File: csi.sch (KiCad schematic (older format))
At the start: 21 parts, among them J1301 OV5640, SW1301 DPDT, U1301 74LVC1G32, U1302 MIC5504-1.8

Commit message: Add WWAN and WLAN+BT MHF4 coax connectors and antennae symbols to the schematic, remove home and back buttons, reorder sheets so that GNSS is above the haptic motor sheet
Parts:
- C1301: renamed from C1308; value 1uF -> NC
- C1302: renamed from C1310; value 100nF -> NC
- C1303: renamed from C1309; value 1uF -> NC
- R1301: renamed from R1304; value 100k -> NC
- U1301: renamed from U1302; value MIC5504-1.8 -> NC
- renumbered C1301 to C1304, C1302 to C1305, C1303 to C1306, C1304 to C1307, C1305 to C1308, C1307 to C1309, C1306 to C1310, R1301 to R1302, R1302 to R1303, R1303 to R1304, U1301 to U1302
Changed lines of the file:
@@
 DPDT with\nmicrophone
 $Comp
-L R R1301
+L R R1302
 U 1 1 5B1ED51C
 P 7000 2950
-F 0 "R1301" H 7175 3000 50  0000 C CNN
+F 0 "R1302" H 7175 3000 50  0000 C CNN
 F 1 "100k" H 7150 2900 50  0000 C CNN
 F 2 "Resistors_SMD:R_0603" V 6930 2950 50  0001 C CNN
@@
 $EndComp
 $Comp
-L C C1301
+L C C1304
 U 1 1 5B1EAF12
 P 7500 3350
-F 0 "C1301" H 7525 3450 50  0000 L CNN
+F 0 "C1304" H 7525 3450 50  0000 L CNN
 F 1 "10nF" H 7525 3250 50  0000 L CNN
 F 2 "Capacitors_SMD:C_0603" H 7538 3200 50  0001 C CNN
@@
 $EndComp
 $Comp
-L R R1302
+L R R1303
 U 1 1 5B1E9C00
 P 7300 3150
-F 0 "R1302" V 7380 3150 50  0000 C CNN
+F 0 "R1303" V 7380 3150 50  0000 C CNN
 F 1 "100k" V 7200 3150 50  0000 C CNN
 F 2 "Resistors_SMD:R_0603" V 7230 3150 50  0001 C CNN
@@
 $EndComp
 $Comp
-L C C1302
+L C C1305
 U 1 1 5B197A0E
 P 8350 2450
-F 0 "C1302" H 8375 2550 50  0000 L CNN
+F 0 "C1305" H 8375 2550 50  0000 L CNN
 F 1 "100nF" H 8375 2350 50  0000 L CNN
 F 2 "Capacitors_SMD:C_0603" H 8388 2300 50  0001 C CNN
@@
 $EndComp
 $Comp
-L 74LVC1G32 U1301
+L 74LVC1G32 U1302
 U 1 1 5B196213
 P 8700 3050
-F 0 "U1301" H 8700 3100 50  0000 C CNN
+F 0 "U1302" H 8700 3100 50  0000 C CNN
 F 1 "74LVC1G32" H 8700 3000 50  0000 C CNN
 F 2 "" H 8700 3050 50  0001 C CNN
@@
 V_IH(min)=1.26V
 $Comp
-L C C1303
+L C C1306
 U 1 1 5B0F9030
 P 9200 2250
-F 0 "C1303" H 9225 2350 50  0000 L CNN
+F 0 "C1306" H 9225 2350 50  0000 L CNN
 F 1 "100nF" H 9225 2150 50  0000 L CNN
 F 2 "Capacitors_SMD:C_0603" H 9238 2100 50  0001 C CNN
@@
 $EndComp
 $Comp
-L C C1304
+L C C1307
 U 1 1 5B0F8FA9
 P 9450 2250
-F 0 "C1304" H 9450 2350 50  0000 L CNN
+F 0 "C1307" H 9450 2350 50  0000 L CNN
 F 1 "10nF" H 9475 2150 50  0000 L CNN
 F 2 "Capacitors_SMD:C_0603" H 9488 2100 50  0001 C CNN
@@
 $EndComp
 $Comp
-L C C1305
+L C C1308
 U 1 1 5B0F8F0F
 P 9700 2250
-F 0 "C1305" H 9700 2350 50  0000 L CNN
+F 0 "C1308" H 9700 2350 50  0000 L CNN
 F 1 "1nF" H 9725 2150 50  0000 L CNN
 F 2 "Capacitors_SMD:C_0603" H 9738 2100 50  0001 C CNN
@@
 $EndComp
 $Comp
-L C C1306
+L C C1310
 U 1 1 5B0F8E57
 P 9950 2250
-F 0 "C1306" H 9950 2350 50  0000 L CNN
+F 0 "C1310" H 9950 2350 50  0000 L CNN
 F 1 "100pF" H 9950 2150 50  0000 L CNN
 F 2 "Capacitors_SMD:C_0603" H 9988 2100 50  0001 C CNN
@@
 $EndComp
 $Comp
-L C C1307
+L C C1309
 U 1 1 5B2B061C
 P 9750 4450
-F 0 "C1307" H 9775 4550 50  0000 L CNN
+F 0 "C1309" H 9775 4550 50  0000 L CNN
 F 1 "100nF" H 9775 4350 50  0000 L CNN
 F 2 "Capacitors_SMD:C_0603" H 9788 4300 50  0001 C CNN
@@
 OV5640 CMOS Image Sensor Datasheet:\nhttps://cdn.sparkfun.com/datasheets/\nSensors/LightImaging/OV5640_datasheet.pdf
 $Comp
-L MIC5504-1.8YM5 U1302
+L MIC5504-1.8YM5 U1301
 U 1 1 5B313EA0
 P 5300 6400
-F 0 "U1302" H 5125 6725 50  0000 C CNN
-F 1 "MIC5504-1.8" H 5250 6650 50  0000 C CNN
+F 0 "U1301" H 5125 6725 50  0000 C CNN
+F 1 "NC" H 5050 6650 50  0000 C CNN
 F 2 "TO_SOT_Packages_SMD:SOT-23-5" H 5300 6000 50  0001 C CNN
 F 3 "http://ww1.microchip.com/downloads/en/DeviceDoc/MIC550x-300mA-Single-Output-LDO-in-Small-Packages-DS20006006A.pdf" H 5300 6600 50  0001 C CNN
@@
 $EndComp
 $Comp
-L C C1308
+L C C1301
 U 1 1 5B320E3F
 P 4850 6500
-F 0 "C1308" H 4875 6600 50  0000 L CNN
-F 1 "1uF" H 4875 6400 50  0000 L CNN
+F 0 "C1301" H 4875 6600 50  0000 L CNN
+F 1 "NC" H 4875 6400 50  0000 L CNN
 F 2 "Capacitors_SMD:C_0603" H 4888 6350 50  0001 C CNN
 F 3 "" H 4850 6500 50  0001 C CNN
@@
 $EndComp
 $Comp
-L C C1309
+L C C1303
 U 1 1 5B320EA7
 P 5900 6500
-F 0 "C1309" H 5925 6600 50  0000 L CNN
-F 1 "1uF" H 5925 6400 50  0000 L CNN
+F 0 "C1303" H 5925 6600 50  0000 L CNN
+F 1 "NC" H 5925 6400 50  0000 L CNN
 F 2 "Capacitors_SMD:C_0603" H 5938 6350 50  0001 C CNN
 F 3 "" H 5900 6500 50  0001 C CNN
@@
 TODO:\nTest if needed
 $Comp
-L C C1310
+L C C1302
 U 1 1 5B3A47C5
 P 5750 6750
-F 0 "C1310" H 5775 6850 50  0000 L CNN
-F 1 "100nF" H 5775 6650 50  0000 L CNN
+F 0 "C1302" H 5775 6850 50  0000 L CNN
+F 1 "NC" H 5775 6650 50  0000 L CNN
 F 2 "Capacitors_SMD:C_0603" H 5788 6600 50  0001 C CNN
 F 3 "" H 5750 6750 50  0001 C CNN
@@
 $EndComp
 $Comp
-L R R1304
+L R R1301
 U 1 1 5B3A4C79
 P 5750 6100
-F 0 "R1304" H 5925 6150 50  0000 C CNN
-F 1 "100k" H 5900 6050 50  0000 C CNN
+F 0 "R1301" H 5925 6150 50  0000 C CNN
+F 1 "NC" H 5900 6050 50  0000 C CNN
 F 2 "Resistors_SMD:R_0603" V 5680 6100 50  0001 C CNN
 F 3 "" H 5750 6100 50  0001 C CNN
@@
 5ms≤RC≤20ms
 $Comp
-L R R1303
+L R R1304
 U 1 1 5B3A721A
 P 9700 3800
-F 0 "R1303" H 9875 3850 50  0000 C CNN
+F 0 "R1304" H 9875 3850 50  0000 C CNN
 F 1 "10k" H 9825 3750 50  0000 C CNN
 F 2 "Resistors_SMD:R_0603" V 9630 3800 50  0001 C CNN

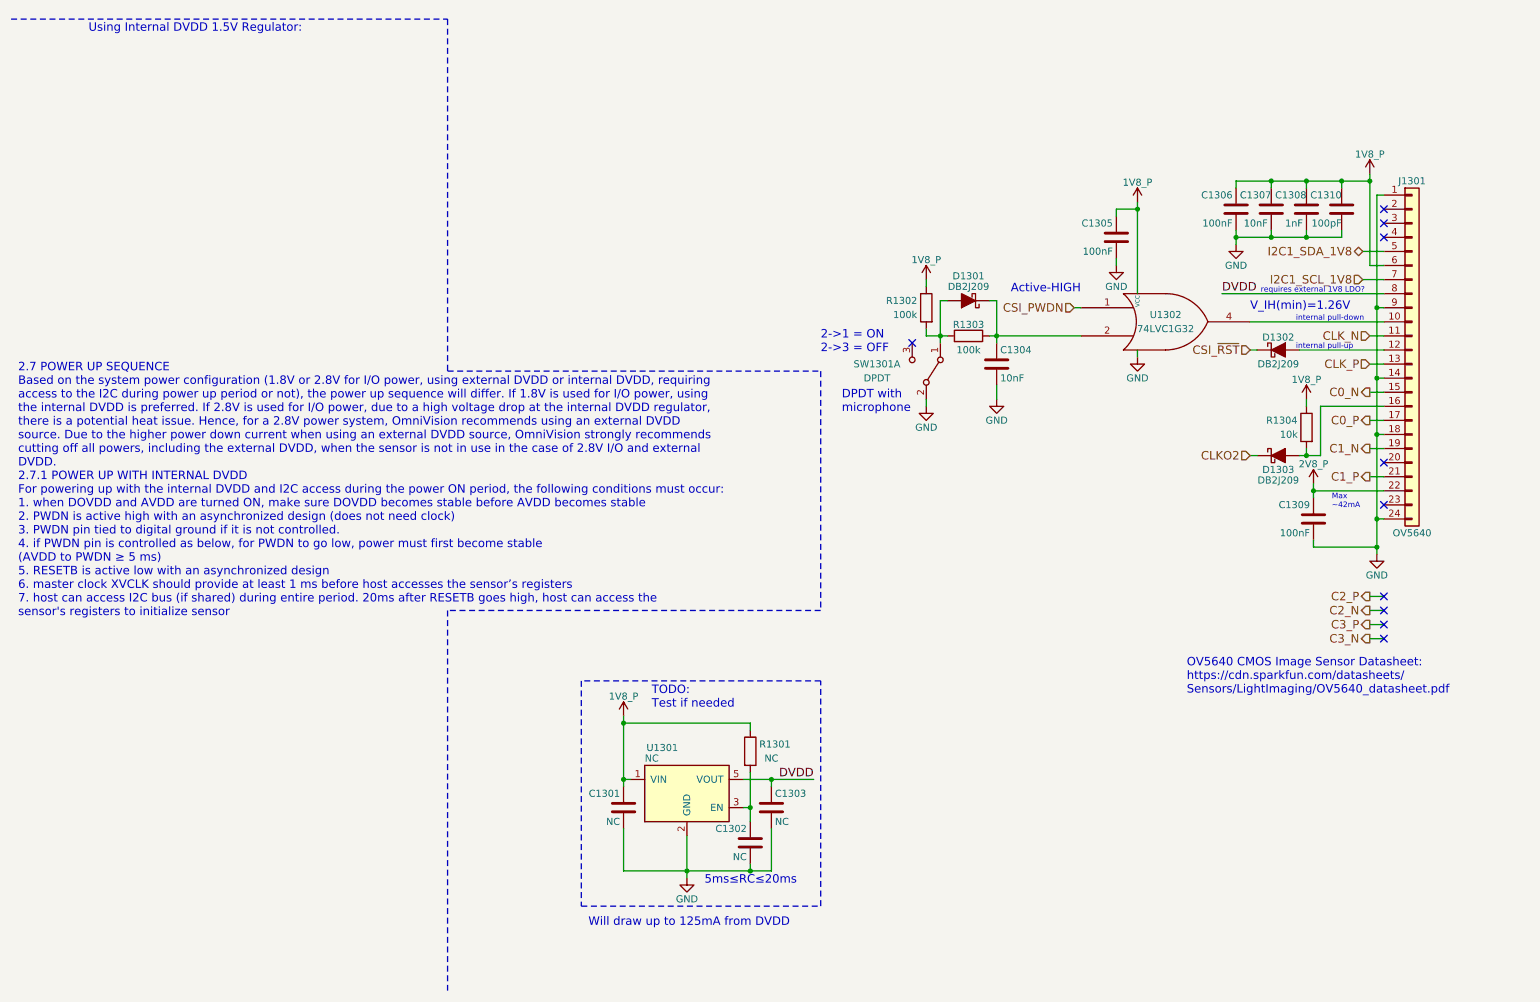
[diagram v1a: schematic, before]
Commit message: Modify the CSI circuit to use a 02x15 connector for potential use with the CO8725-B5SA-E camera, include cap touch FPC connector details, make minor adjustments to GNSS antenna circuit
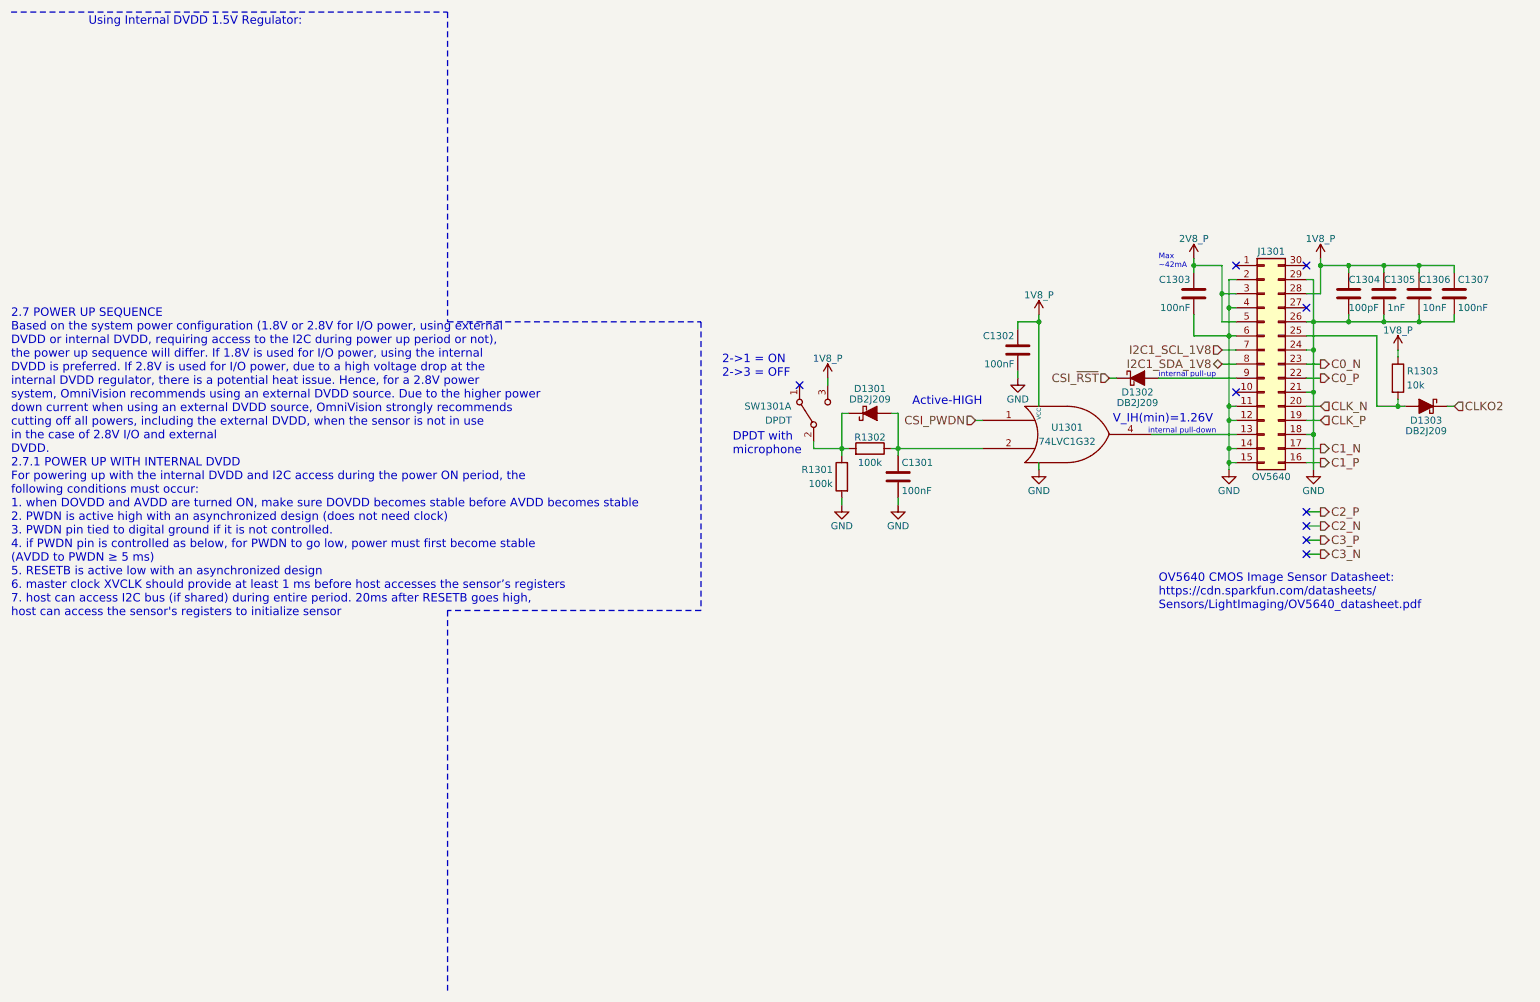
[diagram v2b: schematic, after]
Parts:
- removed C1301, C1302, C1303: NC, Capacitors_SMD:C_0603, symbol C
- removed J1301: OV5640, symbol Conn_01x24
- removed R1301: NC, Resistors_SMD:R_0603, symbol R
- removed U1301: NC, TO_SOT_Packages_SMD:SOT-23-5, symbol MIC5504-1.8YM5
- added J1301: OV5640, symbol Conn_02x15_Counter_Clockwise
- C1301: renamed from C1304; value 10nF -> 100nF
- renumbered C1305 to C1302, C1309 to C1303, C1310 to C1304, C1308 to C1305, C1307 to C1306, C1306 to C1307, R1302 to R1301, R1303 to R1302, R1304 to R1303, U1302 to U1301
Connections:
- net 1V8_P: now also SW1301.3 (C), J1301.28 (Pin_28); no longer R1301.1
- net 2V8_P: now also J1301.3 (Pin_3), J1301.5 (Pin_5)
- net C0_N: now also J1301.23 (Pin_23)
- net C0_P: now also J1301.22 (Pin_22)
- net C1_N: now also J1301.17 (Pin_17)
- net C1_P: now also J1301.16 (Pin_16)
- net CLK_N: now also J1301.20 (Pin_20)
- net CLK_P: now also J1301.19 (Pin_19)
- net GND: now also R1301.2, J1301.11 (Pin_11), J1301.12 (Pin_12), J1301.14 (Pin_14), J1301.15 (Pin_15), J1301.18 (Pin_18), J1301.2 (Pin_2), J1301.21 (Pin_21), J1301.24 (Pin_24), J1301.26 (Pin_26), J1301.29 (Pin_29), J1301.4 (Pin_4), J1301.6 (Pin_6); no longer SW1301.2 (B)
- net I2C1_SCL_1V8: now also J1301.7 (Pin_7)
- net I2C1_SDA_1V8: now also J1301.8 (Pin_8)
- net at U1301.4: now also J1301.13 (Pin_13)
- net at D1302.2 (A): now also J1301.9 (Pin_9)
- net at D1303.2 (A), R1303.2: now also J1301.25 (Pin_25)
- net at C1301.1, R1302.1, U1301.2: now also D1301.2 (A); no longer D1301.1 (K)
- new net: D1301.1 (K), R1301.1, R1302.2, SW1301.2 (B)
- now unconnected: SW1301.1 (A)
- no-connect marks 10 -> 9
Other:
- note added: "2.7 POWER UP SEQUENCE\nBased on the system power configuration (1.8V or 2.8V for I/O power, using external\nDVDD or internal DVDD, requiring access to the I2C during power up period or not),\nthe power up sequence will differ. If 1.8V is used for I/O power, using the internal\nDVDD is preferred. If 2.8V is used for I/O power, due to a high voltage drop at the\ninternal DVDD regulator, there is a 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"
- note removed: "2.7 POWER UP SEQUENCE\nBased on the system power configuration (1.8V or 2.8V for I/O power, using external DVDD or internal DVDD, requiring\naccess to the I2C during power up period or not), the power up sequence will differ. If 1.8V is used for I/O power, using\nthe internal DVDD is preferred. If 2.8V is used for I/O power, due to a high voltage drop at the internal DVDD regulator,\nthere is a p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"
- note removed: "5ms≤RC≤20ms"
- note removed: "TODO:\nTest if needed"
- note removed: "Will draw up to 125mA from DVDD"
- note removed: "requires external 1V8 LDO?"
- moved on the sheet: C1301, C1302, C1303, C1304, C1305, C1306, C1307, D1301, D1302, D1303, R1301, R1302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

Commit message: Include address in schematic notes for all I2C1 slaves, make HDMI connector shielding resistor to GND 0Ohms
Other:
- note added: "Slave Address: 0x78"
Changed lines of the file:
@@
 	10750 3050 10750 3000
 Connection ~ 10000 3050
+Text Notes 9000 2300 0    60   ~ 0
+Slave Address: 0x78
 $EndSCHEMATC

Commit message: Add notes regarding I2C's 3V3_OUT supply and the fact that it is sourced from NVCC_3P3 (3A BUCK6), add additional notes regarding the RTC and Camera's I2C slave address, reannotate the whole schematic (nearly the last time)
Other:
- note added: "7-bit Slave Address: 0x78\n (1111 000x)"
- note added: "Read: 0xF1\nWrite 0xF0"
- note removed: "Slave Address: 0x78"
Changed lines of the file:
@@
 Sheet 13 24
 Title ""
-Date "2018-05-23"
+Date "2018-05-31"
 Rev "v0.1.0"
 Comp "Purism SPC"
@@
 $EndComp
 $Comp
-L GND #PWR0194
+L GND #PWR1303
 U 1 1 5B1EAF19
 P 6800 4350
-F 0 "#PWR0194" H 6800 4100 50  0001 C CNN
+F 0 "#PWR1303" H 6800 4100 50  0001 C CNN
 F 1 "GND" H 6800 4200 50  0000 C CNN
 F 2 "" H 6800 4350 50  0001 C CNN
@@
 $EndComp
 $Comp
-L 1V8_P #PWR0195
+L 1V8_P #PWR1301
 U 1 1 5B1DBE6F
 P 6300 3450
-F 0 "#PWR0195" H 6300 3300 50  0001 C CNN
+F 0 "#PWR1301" H 6300 3300 50  0001 C CNN
 F 1 "1V8_P" H 6300 3590 50  0000 C CNN
 F 2 "" H 6300 3450 50  0001 C CNN
@@
 $EndComp
 $Comp
-L GND #PWR0196
+L GND #PWR1304
 U 1 1 5B1A278C
 P 7650 3450
-F 0 "#PWR0196" H 7650 3200 50  0001 C CNN
+F 0 "#PWR1304" H 7650 3200 50  0001 C CNN
 F 1 "GND" H 7650 3300 50  0000 C CNN
 F 2 "" H 7650 3450 50  0001 C CNN
@@
 $EndComp
 $Comp
-L GND #PWR0197
+L GND #PWR1306
 U 1 1 5B1964B5
 P 7800 4100
-F 0 "#PWR0197" H 7800 3850 50  0001 C CNN
+F 0 "#PWR1306" H 7800 3850 50  0001 C CNN
 F 1 "GND" H 7800 3950 50  0000 C CNN
 F 2 "" H 7800 4100 50  0001 C CNN
@@
 CLKO2
 $Comp
-L 1V8_P #PWR0198
+L 1V8_P #PWR1311
 U 1 1 5B105CDE
 P 10350 3250
-F 0 "#PWR0198" H 10350 3100 50  0001 C CNN
+F 0 "#PWR1311" H 10350 3100 50  0001 C CNN
 F 1 "1V8_P" H 10350 3390 50  0000 C CNN
 F 2 "" H 10350 3250 50  0001 C CNN
@@
 $EndComp
 $Comp
-L 1V8_P #PWR0199
+L 1V8_P #PWR1310
 U 1 1 5B0F8E1D
 P 9800 2600
-F 0 "#PWR0199" H 9800 2450 50  0001 C CNN
+F 0 "#PWR1310" H 9800 2450 50  0001 C CNN
 F 1 "1V8_P" H 9800 2740 50  0000 C CNN
 F 2 "" H 9800 2600 50  0001 C CNN
@@
 C0_P
 $Comp
-L 1V8_P #PWR0200
+L 1V8_P #PWR1305
 U 1 1 5B19049B
 P 7800 3000
-F 0 "#PWR0200" H 7800 2850 50  0001 C CNN
+F 0 "#PWR1305" H 7800 2850 50  0001 C CNN
 F 1 "1V8_P" H 7800 3140 50  0000 C CNN
 F 2 "" H 7800 3000 50  0001 C CNN
@@
 $EndComp
 $Comp
-L 2V8_P #PWR0201
+L 2V8_P #PWR1307
 U 1 1 5B2B0429
 P 8900 2600
-F 0 "#PWR0201" H 8900 2450 50  0001 C CNN
+F 0 "#PWR1307" H 8900 2450 50  0001 C CNN
 F 1 "2V8_P" H 8900 2740 50  0000 C CNN
 F 2 "" H 8900 2600 50  0001 C CNN
@@
 NoConn ~ 9200 2650
 $Comp
-L GND #PWR0202
+L GND #PWR1308
 U 1 1 5B11F1A4
 P 9150 4100
-F 0 "#PWR0202" H 9150 3850 50  0001 C CNN
+F 0 "#PWR1308" H 9150 3850 50  0001 C CNN
 F 1 "GND" H 9150 3950 50  0000 C CNN
 F 2 "" H 9150 4100 50  0001 C CNN
@@
 NoConn ~ 9200 3550
 $Comp
-L GND #PWR0203
+L GND #PWR1309
 U 1 1 5B11FD52
 P 9750 4100
-F 0 "#PWR0203" H 9750 3850 50  0001 C CNN
+F 0 "#PWR1309" H 9750 3850 50  0001 C CNN
 F 1 "GND" H 9750 3950 50  0000 C CNN
 F 2 "" H 9750 4100 50  0001 C CNN
@@
 	9800 2600 9800 2850
 $Comp
-L GND #PWR0204
+L GND #PWR1302
 U 1 1 5B164232
 P 6400 4350
-F 0 "#PWR0204" H 6400 4100 50  0001 C CNN
+F 0 "#PWR1302" H 6400 4100 50  0001 C CNN
 F 1 "GND" H 6400 4200 50  0000 C CNN
 F 2 "" H 6400 4350 50  0001 C CNN
@@
 	10750 3050 10750 3000
 Connection ~ 10000 3050
-Text Notes 9000 2300 0    60   ~ 0
-Slave Address: 0x78
+Text Notes 8850 2150 0    60   ~ 0
+7-bit Slave Address: 0x78\n       (1111 000x)
+Text Notes 9200 2400 0    60   ~ 0
+Read: 0xF1\nWrite 0xF0
 $EndSCHEMATC

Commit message: Assign most of the capacitors their respective footprints (most are 0603s), add camera/CSI connector component info, source cheaper distributors for 3.5mm headset jack and RJ45
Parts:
- J1301: Distrib Link (none) -> https://www.mouser.com/ProductDetail/Panasonic-Industrial-D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; Distrib PN (none) -> 769-AXT630124; MFG Name (none) -> Panasonic; MFG Part Num (none) -> AXT630124; Others (none) -> https://octopart.com/search?q=AXT630124&start=0; Tolerance (none) -> -
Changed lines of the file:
@@
 $EndComp
 $Comp
-L GND #PWR1303
+L GND #PWR0194
 U 1 1 5B1EAF19
 P 6800 4350
-F 0 "#PWR1303" H 6800 4100 50  0001 C CNN
+F 0 "#PWR0194" H 6800 4100 50  0001 C CNN
 F 1 "GND" H 6800 4200 50  0000 C CNN
 F 2 "" H 6800 4350 50  0001 C CNN
@@
 $EndComp
 $Comp
-L 1V8_P #PWR1301
+L 1V8_P #PWR0195
 U 1 1 5B1DBE6F
 P 6300 3450
-F 0 "#PWR1301" H 6300 3300 50  0001 C CNN
+F 0 "#PWR0195" H 6300 3300 50  0001 C CNN
 F 1 "1V8_P" H 6300 3590 50  0000 C CNN
 F 2 "" H 6300 3450 50  0001 C CNN
@@
 $EndComp
 $Comp
-L GND #PWR1304
+L GND #PWR0196
 U 1 1 5B1A278C
 P 7650 3450
-F 0 "#PWR1304" H 7650 3200 50  0001 C CNN
+F 0 "#PWR0196" H 7650 3200 50  0001 C CNN
 F 1 "GND" H 7650 3300 50  0000 C CNN
 F 2 "" H 7650 3450 50  0001 C CNN
@@
 $EndComp
 $Comp
-L GND #PWR1306
+L GND #PWR0197
 U 1 1 5B1964B5
 P 7800 4100
-F 0 "#PWR1306" H 7800 3850 50  0001 C CNN
+F 0 "#PWR0197" H 7800 3850 50  0001 C CNN
 F 1 "GND" H 7800 3950 50  0000 C CNN
 F 2 "" H 7800 4100 50  0001 C CNN
@@
 CLKO2
 $Comp
-L 1V8_P #PWR1311
+L 1V8_P #PWR0198
 U 1 1 5B105CDE
 P 10350 3250
-F 0 "#PWR1311" H 10350 3100 50  0001 C CNN
+F 0 "#PWR0198" H 10350 3100 50  0001 C CNN
 F 1 "1V8_P" H 10350 3390 50  0000 C CNN
 F 2 "" H 10350 3250 50  0001 C CNN
@@
 $EndComp
 $Comp
-L 1V8_P #PWR1310
+L 1V8_P #PWR0199
 U 1 1 5B0F8E1D
 P 9800 2600
-F 0 "#PWR1310" H 9800 2450 50  0001 C CNN
+F 0 "#PWR0199" H 9800 2450 50  0001 C CNN
 F 1 "1V8_P" H 9800 2740 50  0000 C CNN
 F 2 "" H 9800 2600 50  0001 C CNN
@@
 C0_P
 $Comp
-L 1V8_P #PWR1305
+L 1V8_P #PWR0200
 U 1 1 5B19049B
 P 7800 3000
-F 0 "#PWR1305" H 7800 2850 50  0001 C CNN
+F 0 "#PWR0200" H 7800 2850 50  0001 C CNN
 F 1 "1V8_P" H 7800 3140 50  0000 C CNN
 F 2 "" H 7800 3000 50  0001 C CNN
@@
 $EndComp
 $Comp
-L 2V8_P #PWR1307
+L 2V8_P #PWR0201
 U 1 1 5B2B0429
 P 8900 2600
-F 0 "#PWR1307" H 8900 2450 50  0001 C CNN
+F 0 "#PWR0201" H 8900 2450 50  0001 C CNN
 F 1 "2V8_P" H 8900 2740 50  0000 C CNN
 F 2 "" H 8900 2600 50  0001 C CNN
@@
 F 1 "OV5640" H 9450 2550 50  0000 C CNN
 F 2 "" H 9400 3350 50  0001 C CNN
-F 3 "" H 9400 3350 50  0001 C CNN
+F 3 "https://www3.panasonic.biz/ac/cdn/e/control/connector/base-fpc/catalog/con_eng_f4s.pdf" H 9400 3350 50  0001 C CNN
+F 4 "Panasonic" H 9400 3350 60  0001 C CNN "MFG Name"
+F 5 "AXT630124" H 9400 3350 60  0001 C CNN "MFG Part Num"
+F 6 "769-AXT630124" H 9400 3350 60  0001 C CNN "Distrib PN"
+F 7 "https://www.mouser.com/ProductDetail/Panasonic-Industrial-Devices/AXT630124?qs=%2fha2pyFaduhWgBlnq%2f5GKY1ayWUWO5uKyvuPHSGZuvc%3d" H 9400 3350 60  0001 C CNN "Distrib Link"
+F 8 "-" H 9400 3350 60  0001 C CNN "Tolerance"
+F 9 "https://octopart.com/search?q=AXT630124&start=0" H 9400 3350 60  0001 C CNN "Others"
 	1    9400 3350
 	1    0    0    -1
@@
 NoConn ~ 9200 2650
 $Comp
-L GND #PWR1308
+L GND #PWR0202
 U 1 1 5B11F1A4
 P 9150 4100
-F 0 "#PWR1308" H 9150 3850 50  0001 C CNN
+F 0 "#PWR0202" H 9150 3850 50  0001 C CNN
 F 1 "GND" H 9150 3950 50  0000 C CNN
 F 2 "" H 9150 4100 50  0001 C CNN
@@
 NoConn ~ 9200 3550
 $Comp
-L GND #PWR1309
+L GND #PWR0203
 U 1 1 5B11FD52
 P 9750 4100
-F 0 "#PWR1309" H 9750 3850 50  0001 C CNN
+F 0 "#PWR0203" H 9750 3850 50  0001 C CNN
 F 1 "GND" H 9750 3950 50  0000 C CNN
 F 2 "" H 9750 4100 50  0001 C CNN
@@
 	9800 2600 9800 2850
 $Comp
-L GND #PWR1302
+L GND #PWR0204
 U 1 1 5B164232
 P 6400 4350
-F 0 "#PWR1302" H 6400 4100 50  0001 C CNN
+F 0 "#PWR0204" H 6400 4100 50  0001 C CNN
 F 1 "GND" H 6400 4200 50  0000 C CNN
 F 2 "" H 6400 4350 50  0001 C CNN
